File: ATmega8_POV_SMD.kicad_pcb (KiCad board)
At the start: 2 copper layers, 17.2 x 154.5 mm, 23 parts, among them IC1 ATMEGA8-P, P1 CONN_01X02, Y1 Crystal_Small

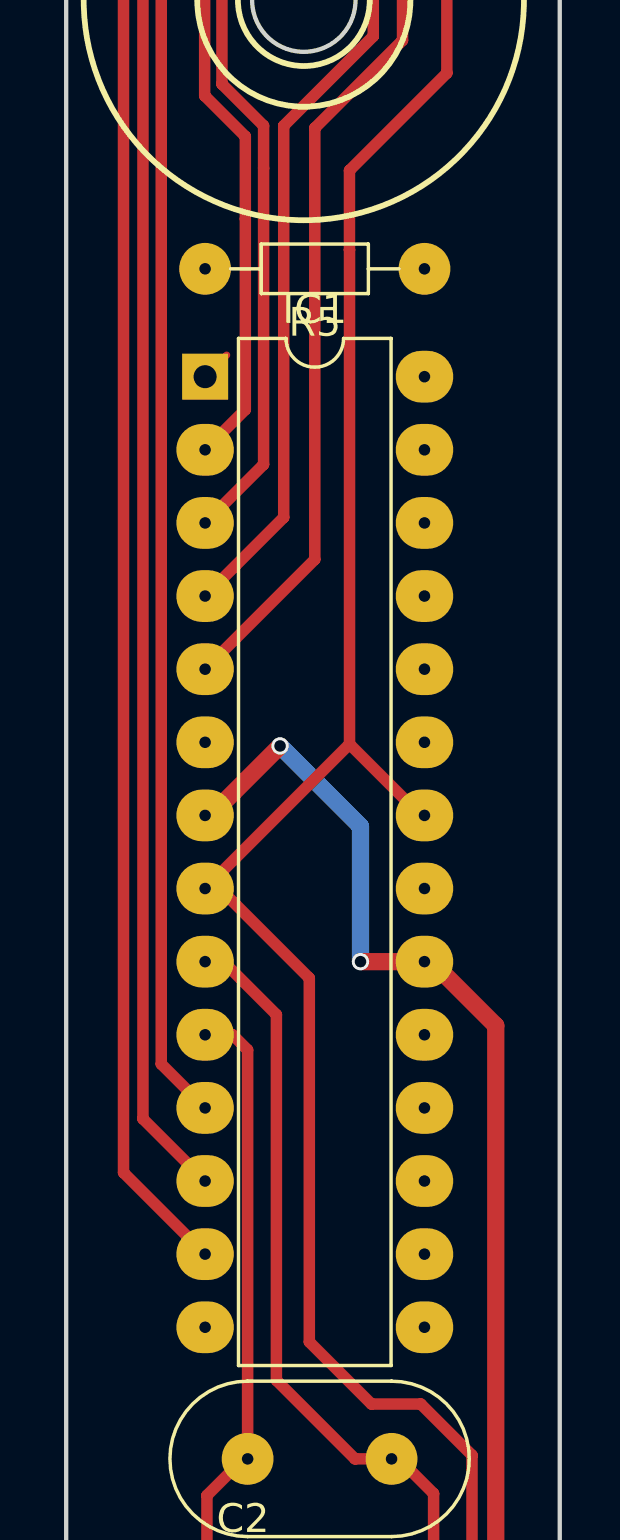
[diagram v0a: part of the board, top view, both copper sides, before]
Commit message: *generating new netlist from new components footprint
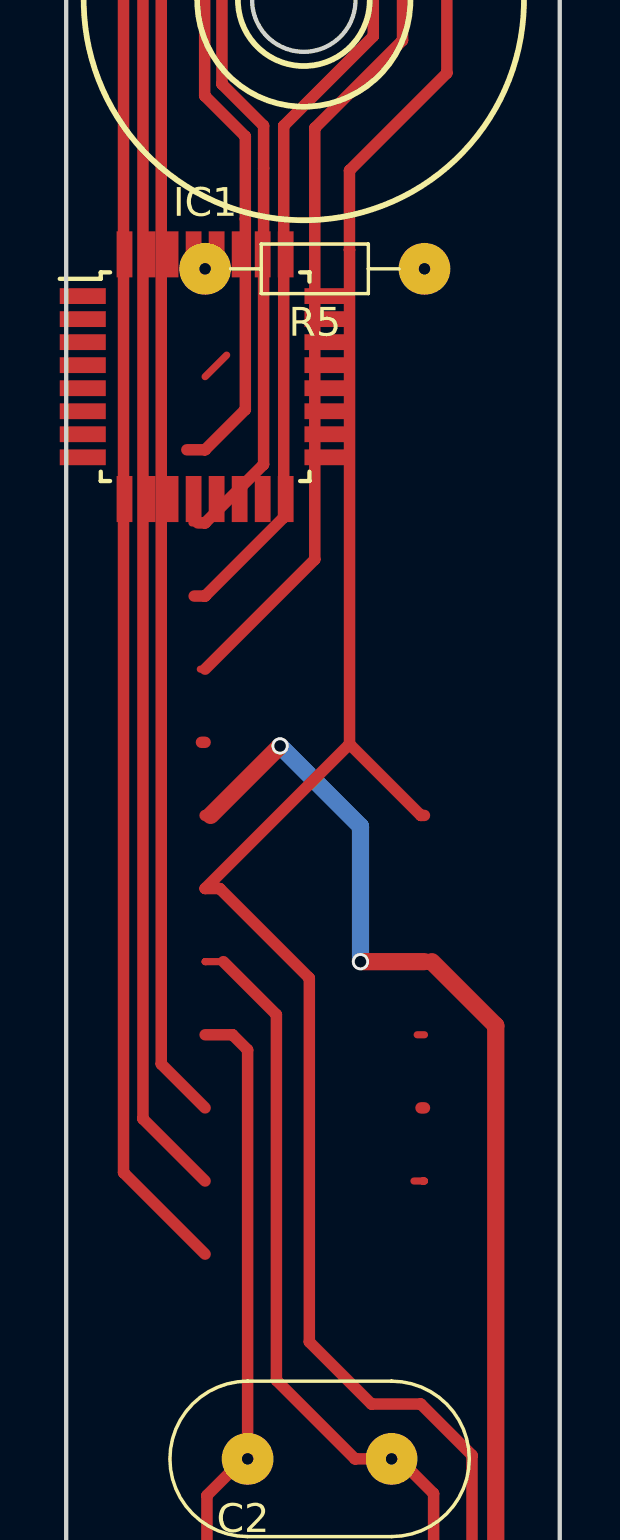
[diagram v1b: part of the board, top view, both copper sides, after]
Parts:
- IC1: footprint Housings_DIP:DIP-28_W7.62mm -> Housings_QFP:TQFP-32_7x7mm_Pitch0.8mm
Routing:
- net (no net): track 0.80 -> 2.13 mm
- net Net-(IC1-Pad1): track 1.06 -> 0.00 mm

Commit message: ~aligning pcb components
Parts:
- removed D10, D11, D12, D9: LED, LEDs:LED_D3.0mm
- removed R10, R11, R12, R13, R14, R15: 1K, Resistors_ThroughHole:R_Axial_DIN0204_L3.6mm_D1.6mm_P7.62mm_Horizontal
- added R1, R2, R3, R4, R6, R7: 1K, Resistors_SMD:R_0805_HandSoldering, F.Cu at (91.4, 83.4)
- C1, C2: footprint Capacitors_ThroughHole:C_Disc_D5.0mm_W2.5mm_P2.50mm -> Capacitors_SMD:C_0805_HandSoldering
- C3: footprint Capacitors_ThroughHole:CP_Radial_D5.0mm_P2.50mm -> Capacitors_Tantalum_SMD:CP_Tantalum_Case-C_EIA-6032-28_Reflow
- R5: value 10K -> 1K; footprint Resistors_ThroughHole:R_Axial_DIN0204_L3.6mm_D1.6mm_P7.62mm_Horizontal -> Resistors_SMD:R_0805_HandSoldering
- R8: footprint Resistors_ThroughHole:R_Axial_DIN0204_L3.6mm_D1.6mm_P7.62mm_Horizontal -> Resistors_SMD:R_0805_HandSoldering
- R9: value 1K -> 10K; footprint Resistors_ThroughHole:R_Axial_DIN0204_L3.6mm_D1.6mm_P7.62mm_Horizontal -> Resistors_SMD:R_0805_HandSoldering
- Y1: footprint Crystals:Resonator-2pin_w10.0mm_h5.0mm -> Crystals:Crystal_C26-LF_d2.1mm_l6.5mm_Vertical
- moved IC1 27.8 mm to (98.0, 170.7)
- moved R5 21.3 mm to (98.0, 160.5)
- moved Y1 2.62 mm to (98.6, 182.9)
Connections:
- R5 pad 1: VCC -> Net-(D5-Pad2)
- R5 pad 2: Net-(IC1-Pad1) -> /D4
- R8 pad 1: Net-(D5-Pad2) -> Net-(D8-Pad2)
- R8 pad 2: /D0 -> /D7
- R9 pad 1: Net-(D6-Pad2) -> VCC
- R9 pad 2: /D1 -> Net-(IC1-Pad1)
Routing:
- net GND: track 175.8 -> 9.70 mm
- net /D7: track 128.5 -> 0.00 mm
- net /D6: track 120.6 -> 0.00 mm
- net /D5: track 112.4 -> 0.00 mm
- net /D3: track 91.8 -> 0.00 mm
- net /D2: track 85.3 -> 0.00 mm
- net /D1: track 72.9 -> 0.00 mm
- net /D0: track 64.7 -> 0.00 mm
- net VCC: track 51.8 -> 8.46 mm, vias 2 -> 0
- net Net-(C1-Pad1): track 26.6 -> 0.00 mm
- net Net-(C2-Pad1): track 22.9 -> 0.00 mm
- net Net-(D12-Pad2): track 3.38 -> 0.00 mm
- net Net-(D10-Pad2): track 3.36 -> 0.00 mm
- net Net-(D9-Pad2): track 3.29 -> 0.00 mm
- net Net-(D11-Pad2): track 3.27 -> 0.00 mm
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
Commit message: ~finalized pcb layout
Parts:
- added D1: LED, LEDs:LED_D3.0mm, F.Cu at (101.6, 88.9)
- added D2: LED, LEDs:LED_D3.0mm, F.Cu at (101.6, 82.8)
- added D3: LED, LEDs:LED_D3.0mm, F.Cu at (101.6, 77.2)
- added D4: LED, LEDs:LED_D3.0mm, F.Cu at (101.6, 71.6)
- moved R9 110.4 mm to (103.6, 182.9), turned to 90 degrees
- moved R5 44.7 mm to (96.5, 115.8), turned to 270 degrees
- moved R8 38.7 mm to (90.4, 115.8), turned to 270 degrees
- moved R1 35.1 mm to (104.6, 115.8), turned to 270 degrees
- moved R2 34.4 mm to (102.6, 115.8), turned to 270 degrees
- moved R3 33.7 mm to (100.6, 115.8), turned to 270 degrees
- moved R4 33.3 mm to (98.6, 115.8), turned to 270 degrees
- moved R6 32.6 mm to (94.5, 115.8), turned to 270 degrees
- moved R7 32.5 mm to (92.5, 115.8), turned to 270 degrees
- moved D8 13.5 mm to (101.6, 48.8)
- moved D7 13.0 mm to (101.6, 54.4)
- moved D6 12.5 mm to (101.6, 59.9)
- moved D5 11.5 mm to (101.6, 66.0)
- moved P1 9.48 mm to (100.6, 184.9)
- moved C1 8.61 mm to (93.5, 182.9), turned to 270 degrees
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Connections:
- R1 pad 1: (no net) -> Net-(D1-Pad2)
- R2 pad 1: (no net) -> Net-(D2-Pad2)
- R3 pad 1: (no net) -> Net-(D3-Pad2)
- R4 pad 1: (no net) -> Net-(D4-Pad2)
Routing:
- net GND: track 9.70 -> 151.7 mm, vias 0 -> 4
- net Net-(D8-Pad2): track 0.04 -> 69.3 mm
- net Net-(D7-Pad2): track 0.36 -> 63.2 mm
- net Net-(D6-Pad2): track 0.36 -> 57.3 mm
- net /D4: track 0.00 -> 54.0 mm
- net /D7: track 0.00 -> 52.7 mm
- net /D0: track 0.00 -> 52.6 mm
- net /D1: track 0.00 -> 52.3 mm
- net /D6: track 0.00 -> 52.3 mm
- net /D2: track 0.00 -> 52.1 mm
- net /D5: track 0.00 -> 52.0 mm
- net /D3: track 0.00 -> 51.8 mm
- net Net-(D5-Pad2): track 3.77 -> 51.2 mm
- net Net-(D4-Pad2): track 0.00 -> 45.6 mm
- net Net-(D3-Pad2): track 0.00 -> 40.0 mm
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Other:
- outline, holes or cut-outs redrawn

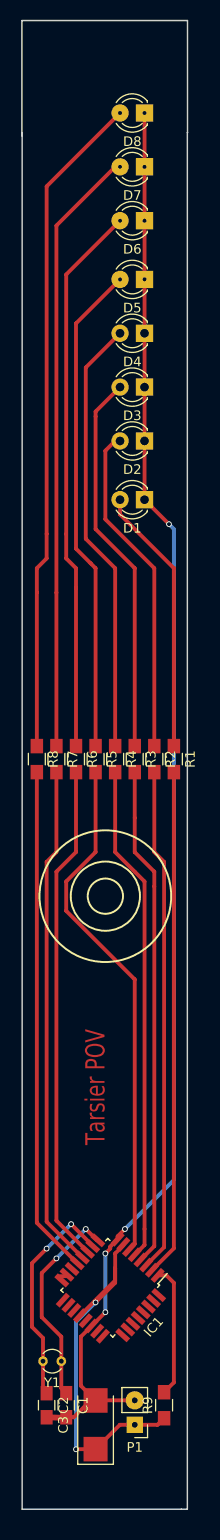
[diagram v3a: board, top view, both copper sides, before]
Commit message: >moving resistors near to IC
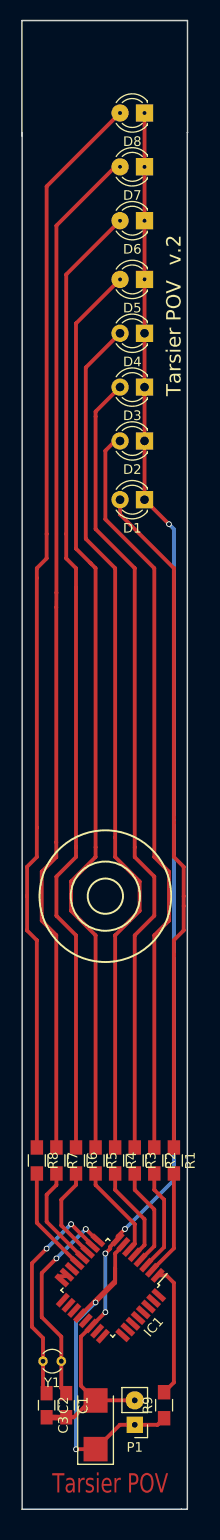
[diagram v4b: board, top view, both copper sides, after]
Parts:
- moved R1 41.7 mm to (104.6, 157.5)
- moved R2 41.7 mm to (102.6, 157.5)
- moved R3 41.7 mm to (100.6, 157.5)
- moved R4 41.7 mm to (98.6, 157.5)
- moved R5 41.7 mm to (96.5, 157.5)
- moved R6 41.7 mm to (94.5, 157.5)
- moved R7 41.7 mm to (92.5, 157.5)
- moved R8 41.7 mm to (90.4, 157.5)
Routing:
- net /D4: track 54.0 -> 9.82 mm
- net Net-(D5-Pad2): track 51.2 -> 94.9 mm
- net Net-(D4-Pad2): track 45.6 -> 89.3 mm
- net Net-(D6-Pad2): track 57.3 -> 100.6 mm
- net Net-(D3-Pad2): track 40.0 -> 83.3 mm
- net Net-(D2-Pad2): track 34.7 -> 77.6 mm
- net Net-(D7-Pad2): track 63.2 -> 106.1 mm
- net Net-(D8-Pad2): track 69.3 -> 111.8 mm
- net Net-(D1-Pad2): track 27.9 -> 70.4 mm
- net /D5: track 52.0 -> 9.88 mm
- net /D2: track 52.1 -> 10.4 mm
- net /D7: track 52.7 -> 11.0 mm
- net /D3: track 51.8 -> 10.1 mm
- net /D1: track 52.3 -> 10.7 mm
- net /D0: track 52.6 -> 11.0 mm
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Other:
- board text added: "v.2"

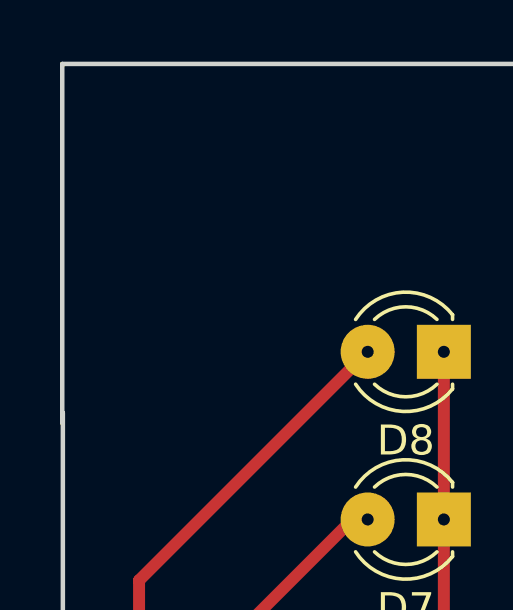
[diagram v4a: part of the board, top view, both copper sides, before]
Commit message: *readme with v2 of prototype board
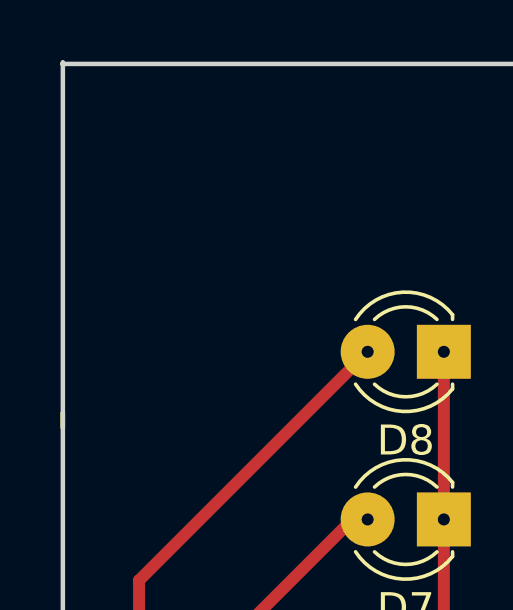
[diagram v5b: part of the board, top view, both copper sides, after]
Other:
- board size 17.2 x 154.5 mm -> 17.2 x 154.6 mm
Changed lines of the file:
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@@
     (links 38)
     (no_connects 0)
-    (area 88.804679 39.096879 106.145401 193.750001)
+    (area 88.804679 39.040999 106.145401 193.750001)
     (thickness 1.6)
     (drawings 14)
@@
     )
   )
+  (gr_line (start 88.9 51.308) (end 88.9 39.116) (angle 90) (layer Edge.Cuts) (width 0.15))
   (gr_text v.2 (at 104.648 62.992 90) (layer F.SilkS)
     (effects (font (size 1.5 1.5) (thickness 0.3)))
@@
   (gr_line (start 106.06024 50.8) (end 106.0704 50.78984) (angle 90) (layer Edge.Cuts) (width 0.15))
   (gr_line (start 106.06024 39.17188) (end 106.06024 50.8) (angle 90) (layer Edge.Cuts) (width 0.15))
-  (gr_line (start 88.87968 51.14544) (end 88.87968 39.17188) (angle 90) (layer Edge.Cuts) (width 0.15))
   (gr_text "Tarsier POV" (at 98.044 191.008) (layer F.Cu)
     (effects (font (size 2 1.5) (thickness 0.375)))

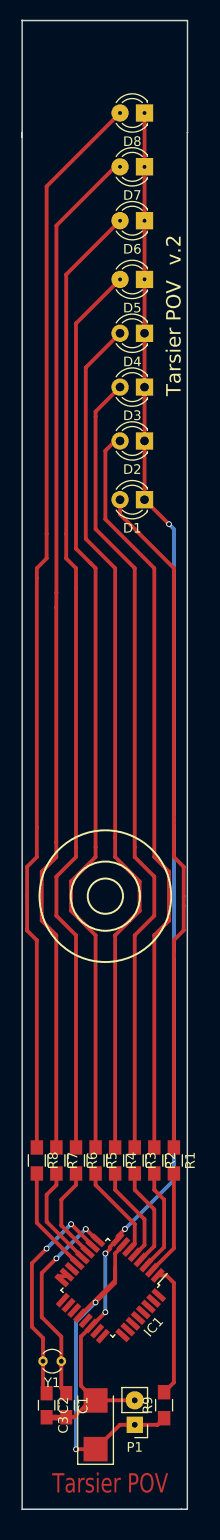
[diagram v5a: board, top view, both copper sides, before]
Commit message: *fix 3D view exception
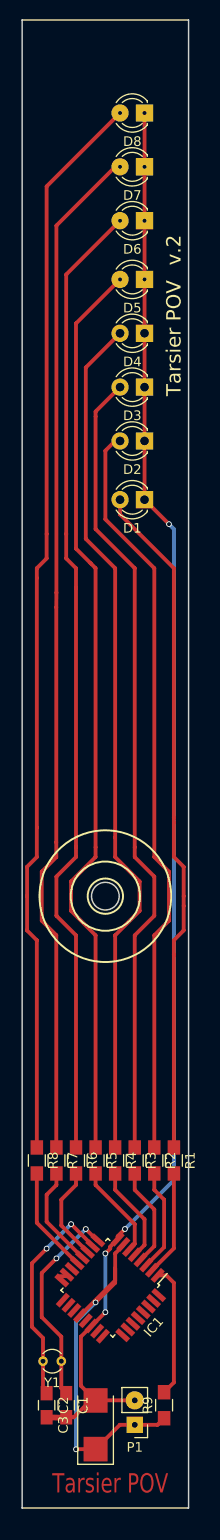
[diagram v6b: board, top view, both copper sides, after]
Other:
- board size 17.2 x 154.6 mm -> 17.3 x 154.4 mm
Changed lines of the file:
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@@
     (area 88.804679 39.040999 106.145401 193.750001)
     (thickness 1.6)
-    (drawings 14)
+    (drawings 13)
     (tracks 197)
     (zones 0)
@@
     )
   )
-  (gr_line (start 88.9 51.308) (end 88.9 39.116) (angle 90) (layer Edge.Cuts) (width 0.15))
+  (gr_line (start 88.9 193.548) (end 106.172 193.548) (angle 90) (layer Edge.Cuts) (width 0.15))
+  (gr_line (start 88.9 39.116) (end 88.9 193.548) (angle 90) (layer Edge.Cuts) (width 0.15))
+  (gr_line (start 106.172 39.116) (end 106.172 193.548) (angle 90) (layer Edge.Cuts) (width 0.15))
+  (gr_line (start 88.9 39.116) (end 106.172 39.116) (angle 90) (layer Edge.Cuts) (width 0.15))
+  (dimension 17.272 (width 0.3) (layer Eco2.User)
+    (gr_text "17.272 mm" (at 97.536 35.734) (layer Eco2.User)
+      (effects (font (size 1.5 1.5) (thickness 0.3)))
+    )
+    (feature1 (pts (xy 88.9 39.116) (xy 88.9 34.384)))
+    (feature2 (pts (xy 106.172 39.116) (xy 106.172 34.384)))
+    (crossbar (pts (xy 106.172 37.084) (xy 88.9 37.084)))
+    (arrow1a (pts (xy 88.9 37.084) (xy 90.026504 36.497579)))
+    (arrow1b (pts (xy 88.9 37.084) (xy 90.026504 37.670421)))
+    (arrow2a (pts (xy 106.172 37.084) (xy 105.045496 36.497579)))
+    (arrow2b (pts (xy 106.172 37.084) (xy 105.045496 37.670421)))
+  )
+  (dimension 154.432 (width 0.3) (layer Eco2.User)
+    (gr_text "154.432 mm" (at 109.554 116.332 90) (layer Eco2.User)
+      (effects (font (size 1.5 1.5) (thickness 0.3)))
+    )
+    (feature1 (pts (xy 106.172 39.116) (xy 110.904 39.116)))
+    (feature2 (pts (xy 106.172 193.548) (xy 110.904 193.548)))
+    (crossbar (pts (xy 108.204 193.548) (xy 108.204 39.116)))
+    (arrow1a (pts (xy 108.204 39.116) (xy 108.790421 40.242504)))
+    (arrow1b (pts (xy 108.204 39.116) (xy 107.617579 40.242504)))
+    (arrow2a (pts (xy 108.204 193.548) (xy 108.790421 192.421496)))
+    (arrow2b (pts (xy 108.204 193.548) (xy 107.617579 192.421496)))
+  )
+  (gr_circle (center 97.536 130.048) (end 98.552 131.064) (layer Edge.Cuts) (width 0.15))
   (gr_text v.2 (at 104.648 62.992 90) (layer F.SilkS)
     (effects (font (size 1.5 1.5) (thickness 0.3)))
@@
   (gr_circle (center 97.536 130.048) (end 102.616 134.62) (layer F.SilkS) (width 0.2))
   (gr_circle (center 97.536 130.048) (end 99.06 131.064) (layer F.SilkS) (width 0.2))
-  (gr_line (start 88.87968 39.17188) (end 106.06024 39.17188) (angle 90) (layer Edge.Cuts) (width 0.15))
-  (gr_line (start 106.06024 50.8) (end 106.0704 50.78984) (angle 90) (layer Edge.Cuts) (width 0.15))
-  (gr_line (start 106.06024 39.17188) (end 106.06024 50.8) (angle 90) (layer Edge.Cuts) (width 0.15))
   (gr_text "Tarsier POV" (at 98.044 191.008) (layer F.Cu)
     (effects (font (size 2 1.5) (thickness 0.375)))
   )
-  (gr_line (start 106.045 193.675) (end 106.045 50.8) (angle 90) (layer Edge.Cuts) (width 0.15))
-  (gr_line (start 105.41 193.675) (end 106.045 193.675) (angle 90) (layer Edge.Cuts) (width 0.15))
-  (gr_line (start 88.9 193.675) (end 105.41 193.675) (angle 90) (layer Edge.Cuts) (width 0.15))
-  (gr_line (start 88.9 50.8) (end 88.9 193.675) (angle 90) (layer Edge.Cuts) (width 0.15))
   (segment (start 92.78 169.488) (end 93.794 169.488) (width 0.4) (layer F.Cu) (net 0))
   (segment (start 96.7592 165.763389) (end 96.675389 165.763389) (width 0.4) (layer F.Cu) (net 1))
